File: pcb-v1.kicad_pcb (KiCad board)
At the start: 2 copper layers, 160 x 96.5 mm, 22 parts, among them J1 Conn_01x03_Socket, J10 Screw_Terminal_01x04, J11 Screw_Terminal_01x04, J12 Screw_Terminal_01x04, J13 Screw_Terminal_01x04, J14 Screw_Terminal_01x06, J15 Conn_01x06_Pin, J2 Conn_01x03_Socket, J3 Conn_01x03_Socket, J4 Conn_01x03_Socket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

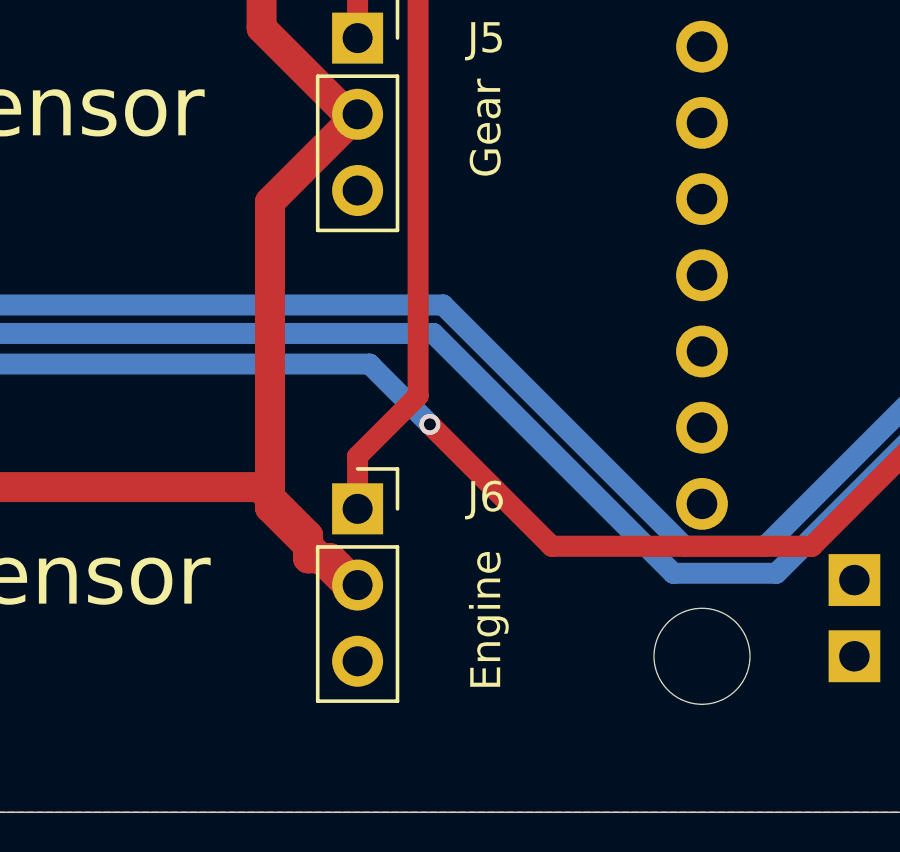
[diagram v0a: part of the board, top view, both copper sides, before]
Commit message: change ground voltage sensor5 not connected
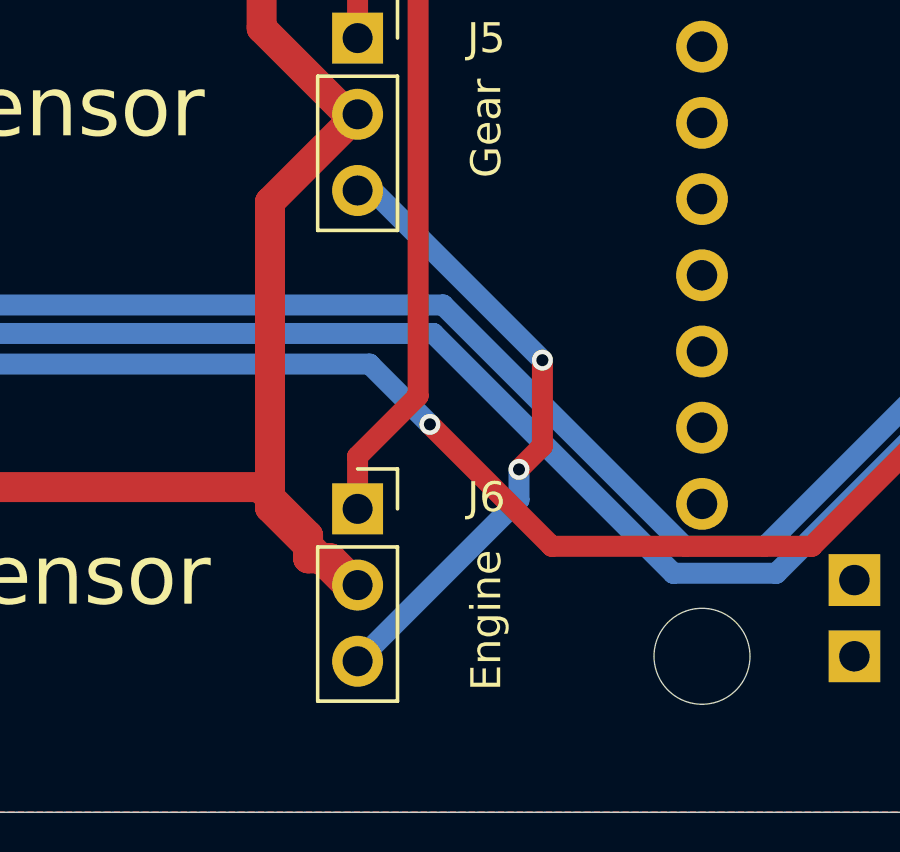
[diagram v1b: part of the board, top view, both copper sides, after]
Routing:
- net GND: track 0.00 -> 21.1 mm, vias 0 -> 2
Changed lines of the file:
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@@
+	)
+	(segment
+		(start 163.67 135.79)
+		(end 162.89 136.57)
+		(width 0.7)
+		(layer "F.Cu")
+		(net "GND")
+	)
+	(segment
+		(start 163.67 132.93)
+		(end 163.67 135.79)
+		(width 0.7)
+		(layer "F.Cu")
+		(net "GND")
+	)
+	(via
+		(at 162.89 136.57)
+		(size 0.7)
+		(drill 0.4)
+		(layers "F.Cu" "B.Cu")
+		(net "GND")
+	)
+	(via
+		(at 163.67 132.93)
+		(size 0.7)
+		(drill 0.4)
+		(layers "F.Cu" "B.Cu")
+		(net "GND")
+	)
+	(segment
+		(start 157.51 127.274)
+		(end 158.014 127.274)
+		(width 0.7)
+		(layer "B.Cu")
+		(net "GND")
+	)
+	(segment
+		(start 162.89 136.57)
+		(end 162.89 137.586)
+		(width 0.7)
+		(layer "B.Cu")
+		(net "GND")
+	)
+	(segment
+		(start 158.014 127.274)
+		(end 163.67 132.93)
+		(width 0.7)
+		(layer "B.Cu")
+		(net "GND")
+	)
+	(segment
+		(start 162.89 137.586)
+		(end 157.51 142.966)
+		(width 0.7)
+		(layer "B.Cu")
+		(net "GND")
 	)
 	(segment
